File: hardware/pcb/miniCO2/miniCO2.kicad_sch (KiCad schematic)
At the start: 11 parts, among them J1 USB_A, SW1 SW_Push, U1 ATSAMD21E18A-M, U2 AP2112K-3.3, U3 SCD40-D-R2

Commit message: Routing finished
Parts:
- D1, D2: footprint LED_SMD:LED_SK6805_PLCC4_2.4x2.7mm_P1.3mm -> miniCO2:LED_SK6805_PLCC4_2.4x2.7mm_P1.3mm
- U1: footprint Package_DFN_QFN:QFN-32-1EP_5x5mm_P0.5mm_EP3.6x3.6mm -> miniCO2:QFN-32-1EP_5x5mm_P0.5mm_EP3.6x3.6mm
- U3: footprint Sensor:Sensirion_SCD4x-1EP_10.1x10.1mm_P1.25mm_EP4.8x4.8mm -> miniCO2:Sensirion_SCD4x-1EP_10.1x10.1mm_P1.25mm_EP4.8x4.8mm
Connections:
- net DIN: now also U1.19 (PA18)
- net SWCLK: now reaches U1.31 (PA30)
- net SWDIO: now reaches U1.32 (PA31)
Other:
- moved on the sheet: SW1

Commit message: Make prototype
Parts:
- added J2: Conn_01x04_Socket, Connector_PinHeader_1.00mm:PinHeader_1x04_P1.00mm_Vertical, symbol Connector:Conn_01x04_Socket
- C1, C2: LCSC Part # (none) -> C2167716
- C3, C4: LCSC Part # (none) -> C5137485
- D1, D2: LCSC Part # (none) -> C2909056
- J1: footprint Connector_USB:917-P81A102ED60200 -> miniCO2:917-P81A102ED60200; LCSC Part # (none) -> C2763086
- SW1: footprint Button_Switch_SMD:LS75C2D-T -> miniCO2:LS75C2D-T; LCSC Part # (none) -> C962551
- U1: LCSC Part # (none) -> C614310
- U2: LCSC Part # (none) -> C51118
- U3: LCSC Part # (none) -> C3659421
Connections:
- net +3.3V: now also J2.1 (Pin_1)
- net GND: now also J2.3 (Pin_3)
- net SWCLK: now also J2.4 (Pin_4)
- net SWDIO: now also J2.2 (Pin_2)
- no-connect marks 0 -> 21

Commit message: Version 1 finished
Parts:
- D1, D2: footprint miniCO2:LED_SK6805_PLCC4_2.4x2.7mm_P1.3mm -> MiniCO2:LED_SK6805_PLCC4_2.4x2.7mm_P1.3mm
- J1: footprint miniCO2:917-P81A102ED60200 -> MiniCO2:917-P81A102ED60200
- J2: footprint Connector_PinHeader_1.00mm:PinHeader_1x04_P1.00mm_Vertical -> MiniCO2:SWD_pogo_pads
- SW1: footprint miniCO2:LS75C2D-T -> MiniCO2:LS75C2D-T
- U1: footprint miniCO2:QFN-32-1EP_5x5mm_P0.5mm_EP3.6x3.6mm -> MiniCO2:QFN-32-1EP_5x5mm_P0.5mm_EP3.6x3.6mm; LCSC Part # C614310 -> C2052801
- U3: footprint miniCO2:Sensirion_SCD4x-1EP_10.1x10.1mm_P1.25mm_EP4.8x4.8mm -> MiniCO2:Sensirion_SCD4x-1EP_10.1x10.1mm_P1.25mm_EP4.8x4.8mm
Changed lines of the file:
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@@
 			)
 		)
-		(property "Footprint" "miniCO2:LED_SK6805_PLCC4_2.4x2.7mm_P1.3mm"
+		(property "Footprint" "MiniCO2:LED_SK6805_PLCC4_2.4x2.7mm_P1.3mm"
 			(at 251.46 104.14 0)
 			(effects
@@
 			)
 		)
-		(property "Footprint" "Connector_PinHeader_1.00mm:PinHeader_1x04_P1.00mm_Vertical"
+		(property "Footprint" "MiniCO2:SWD_pogo_pads"
 			(at 261.62 129.54 0)
 			(effects
@@
 			)
 		)
-		(property "Footprint" "miniCO2:QFN-32-1EP_5x5mm_P0.5mm_EP3.6x3.6mm"
+		(property "Footprint" "MiniCO2:QFN-32-1EP_5x5mm_P0.5mm_EP3.6x3.6mm"
 			(at 165.1 133.35 0)
 			(effects
@@
 			)
 		)
-		(property "LCSC Part #" "C614310"
+		(property "LCSC Part #" "C2052801"
 			(at 130.81 86.36 0)
 			(effects
@@
 			)
 		)
-		(property "Footprint" "miniCO2:917-P81A102ED60200"
+		(property "Footprint" "MiniCO2:917-P81A102ED60200"
 			(at 264.16 30.48 0)
 			(effects
@@
 			)
 		)
-		(property "Footprint" "miniCO2:Sensirion_SCD4x-1EP_10.1x10.1mm_P1.25mm_EP4.8x4.8mm"
+		(property "Footprint" "MiniCO2:Sensirion_SCD4x-1EP_10.1x10.1mm_P1.25mm_EP4.8x4.8mm"
 			(at 260.35 64.77 0)
 			(effects
@@
 			)
 		)
-		(property "Footprint" "miniCO2:LS75C2D-T"
+		(property "Footprint" "MiniCO2:LS75C2D-T"
 			(at 104.14 130.81 0)
 			(effects
@@
 			)
 		)
-		(property "Footprint" "miniCO2:LED_SK6805_PLCC4_2.4x2.7mm_P1.3mm"
+		(property "Footprint" "MiniCO2:LED_SK6805_PLCC4_2.4x2.7mm_P1.3mm"
 			(at 270.51 104.14 0)
 			(effects

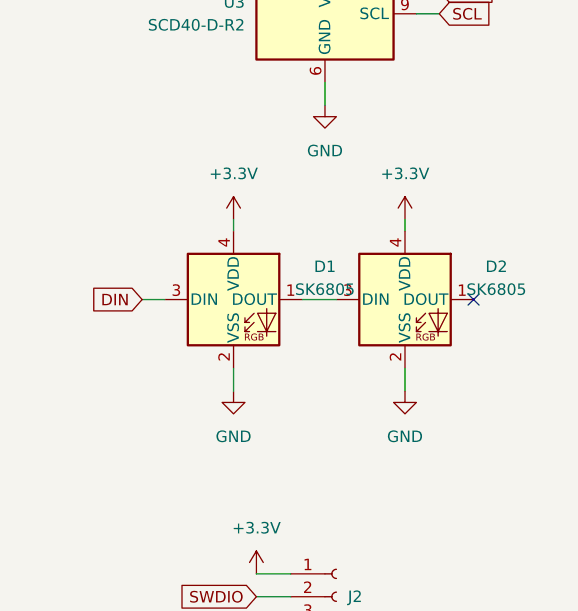
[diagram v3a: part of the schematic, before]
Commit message: Switch to front facing LEDs
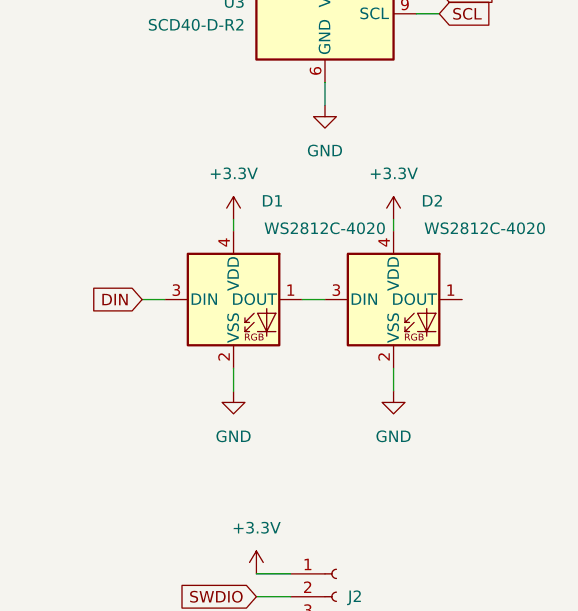
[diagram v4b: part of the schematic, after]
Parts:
- C1, C2: LCSC Part # C2167716 -> C19702
- D1, D2: value SK6805 -> WS2812C-4020; footprint MiniCO2:LED_SK6805_PLCC4_2.4x2.7mm_P1.3mm -> MiniCO2:WS2812C-4020; LCSC Part # C2909056 -> C5149201
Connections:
- no-connect marks 21 -> 20

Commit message: Version 1 finished and sent to production
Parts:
- D1, D2: LCSC Part # C5149201 -> C4154870
- J1: LCSC Part # C2763086 -> C2763083
- U1: value ATSAMD21E18A-M -> ATSAMD21E17A-MUT; LCSC Part # C2052801 -> 3A991A2
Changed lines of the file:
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@@
 			)
 		)
-		(property "LCSC Part #" "C5149201"
+		(property "LCSC Part #" "C4154870"
 			(at 250.19 96.52 0)
 			(effects
@@
 			)
 		)
-		(property "Value" "ATSAMD21E18A-M"
+		(property "Value" "ATSAMD21E17A-MUT"
 			(at 147.32 87.63 0)
 			(effects
@@
 			)
 		)
-		(property "LCSC Part #" "C2052801"
+		(property "LCSC Part #" "3A991A2"
 			(at 130.81 86.36 0)
 			(effects
@@
 			)
 		)
-		(property "LCSC Part #" "C2763086"
+		(property "LCSC Part #" " C2763083"
 			(at 260.35 29.21 0)
 			(effects
@@
 			)
 		)
-		(property "LCSC Part #" "C5149201"
+		(property "LCSC Part #" "C4154870"
 			(at 267.97 96.52 0)
 			(effects

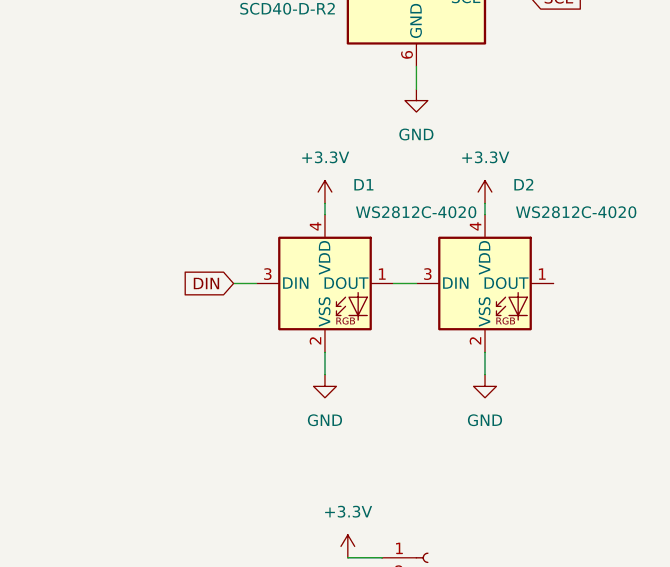
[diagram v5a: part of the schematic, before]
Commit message: Fix D1, D2 footprints
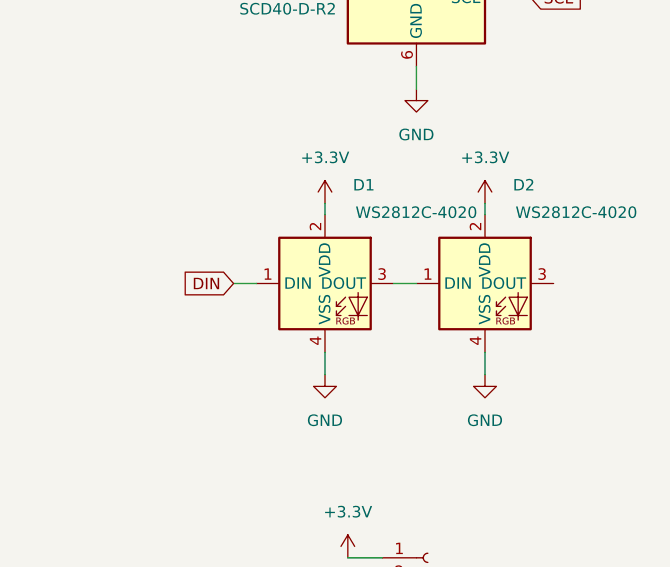
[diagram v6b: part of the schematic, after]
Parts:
- D1, D2: symbol LED:SK6805 -> MiniCO2:WS2812C-4020
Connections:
- net +3.3V: now also D1.2 (VDD), D2.2 (VDD); no longer D1.4 (VDD), D2.4 (VDD)
- net DIN: now also D1.1 (DIN); no longer D1.3 (DIN)
- net GND: now also D1.4 (VSS), D2.4 (VSS); no longer D1.2 (VSS), D2.2 (VSS)
- net at D2.3 (DOUT): no longer D1.1 (DOUT)
- net at D2.1 (DIN): now also D1.3 (DOUT)
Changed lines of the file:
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@@
 	)
 	(symbol
-		(lib_id "LED:SK6805")
+		(lib_id "MiniCO2:WS2812C-4020")
 		(at 250.19 96.52 0)
 		(unit 1)
@@
 		)
 		(property "Footprint" "MiniCO2:WS2812C-4020"
-			(at 251.46 104.14 0)
-			(effects
-				(font
-					(size 1.27 1.27)
-				)
-				(justify left top)
+			(at 250.19 96.52 0)
+			(effects
+				(font
+					(size 1.27 1.27)
+				)
 				(hide yes)
 			)
 		)
 		(property "Datasheet" ""
-			(at 252.73 106.045 0)
-			(effects
-				(font
-					(size 1.27 1.27)
-				)
-				(justify left top)
+			(at 250.19 96.52 0)
+			(effects
+				(font
+					(size 1.27 1.27)
+				)
 				(hide yes)
 			)
@@
 	)
 	(symbol
-		(lib_id "LED:SK6805")
+		(lib_id "MiniCO2:WS2812C-4020")
 		(at 267.97 96.52 0)
 		(unit 1)
@@
 		)
 		(property "Footprint" "MiniCO2:WS2812C-4020"
-			(at 269.24 104.14 0)
-			(effects
-				(font
-					(size 1.27 1.27)
-				)
-				(justify left top)
+			(at 267.97 96.52 0)
+			(effects
+				(font
+					(size 1.27 1.27)
+				)
 				(hide yes)
 			)
 		)
 		(property "Datasheet" ""
-			(at 270.51 106.045 0)
-			(effects
-				(font
-					(size 1.27 1.27)
-				)
-				(justify left top)
-				(hide yes)
-			)
+			(at 267.97 96.52 0)
+			(effects
+				(font
+					(size 1.27 1.27)
+				)
+				(hide yes)
+			)
